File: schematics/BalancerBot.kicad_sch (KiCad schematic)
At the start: 12 parts, among them M3 Motor_Servo, M4 Motor_Servo, SW1 SW_SPDT, SW2 SW_Push, U1 ICM-20948

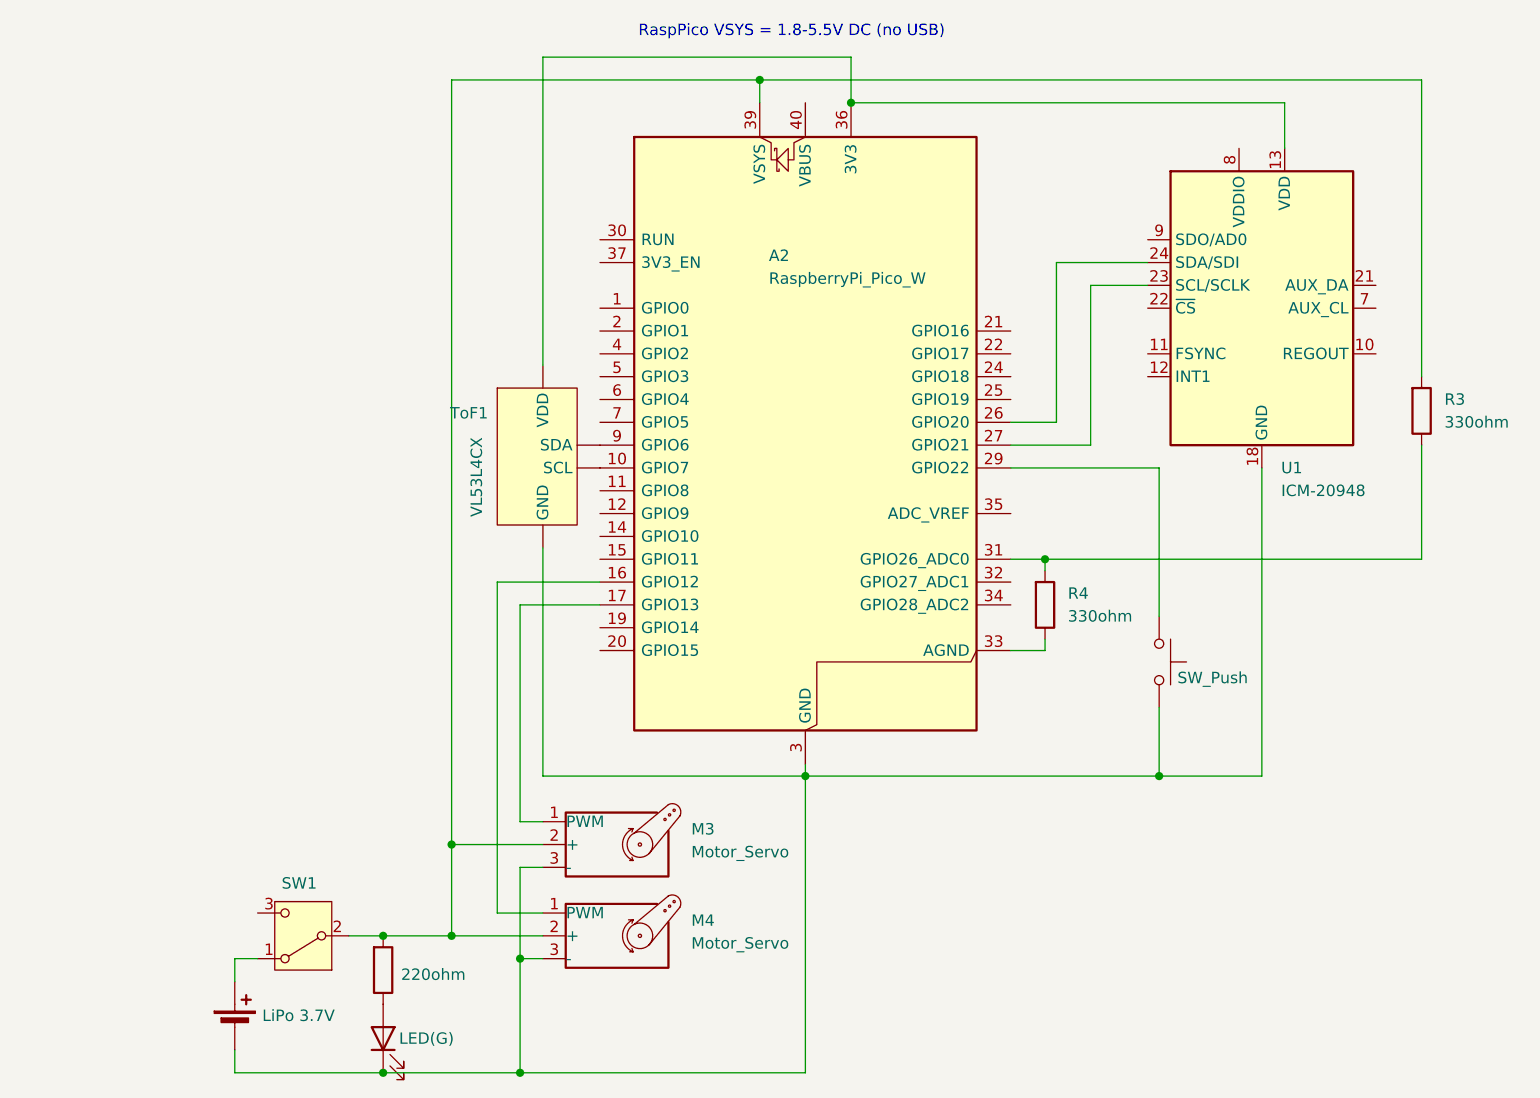
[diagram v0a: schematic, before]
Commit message: Speaker integration
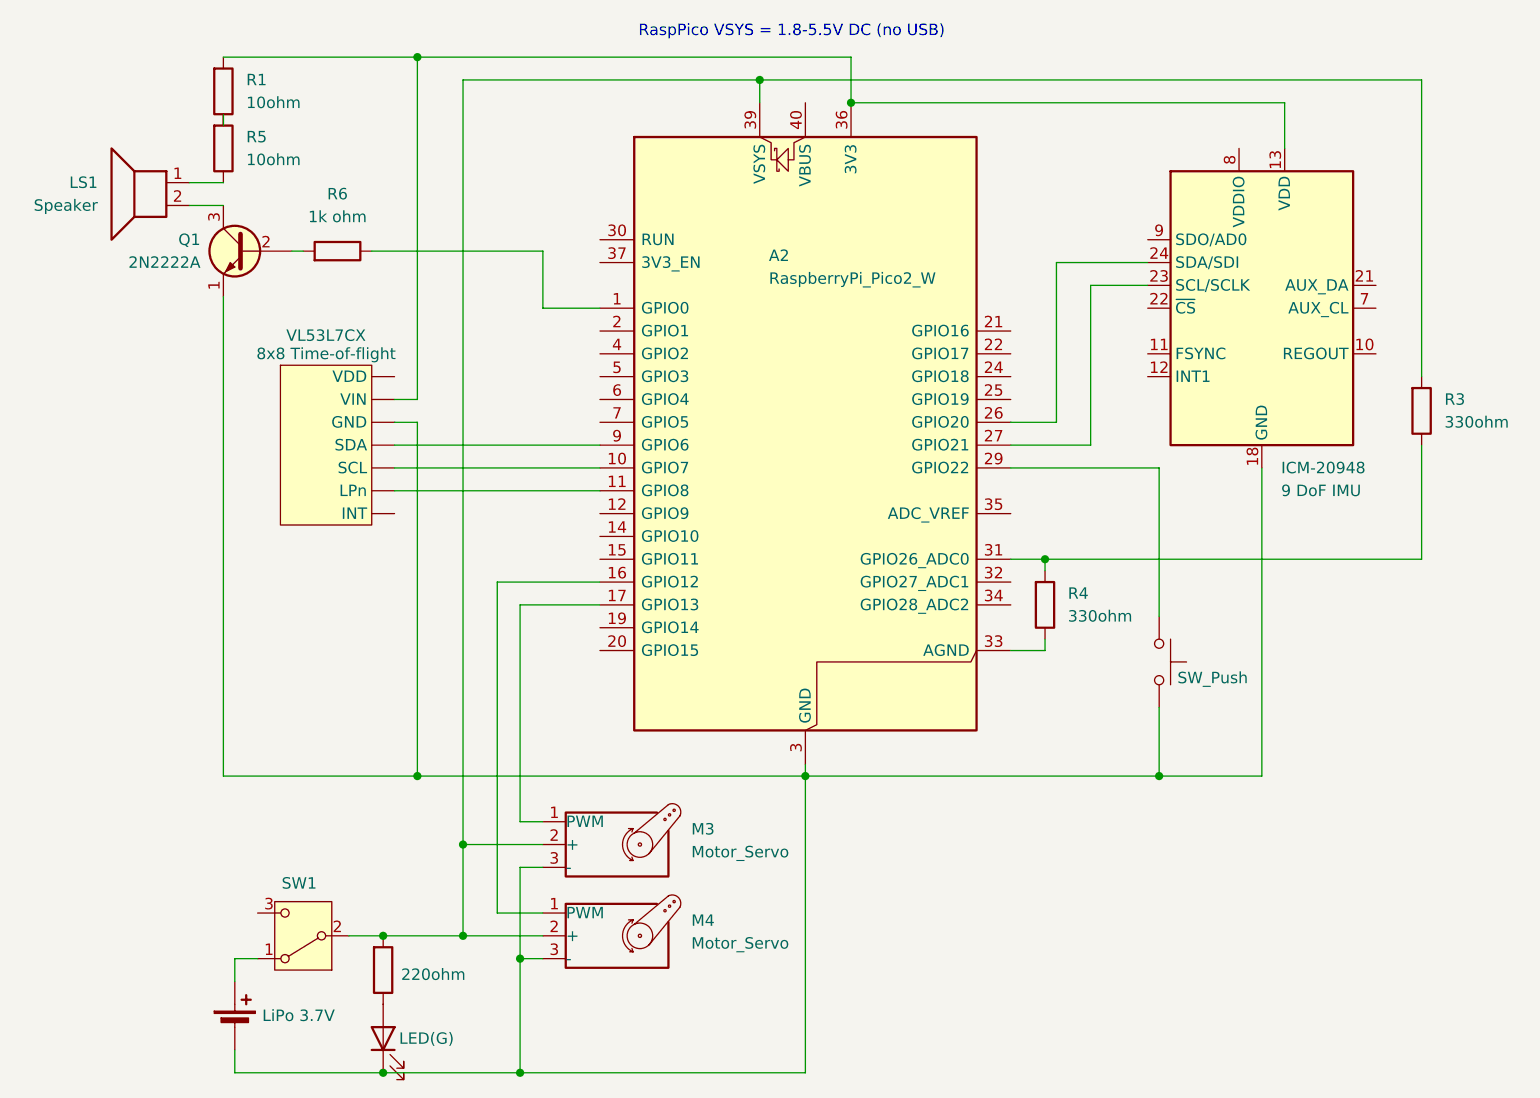
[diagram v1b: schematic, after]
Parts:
- removed ToF1: VL53L4CX, symbol 1MyLibrary:VL53L4CX
- added LS1: Speaker, symbol Device:Speaker
- added Q1: 2N2222A, PCM_Package_TO_SOT_THT_AKL:TO-18-3_EBC, symbol PCM_Transistor_BJT_AKL:2N2222A
- added R1, R5: 10ohm, symbol PCM_Resistor_AKL:R_Generic
- added R6: 1k ohm, symbol PCM_Resistor_AKL:R_Generic
- added VL53L7CX: 8x8 Time-of-flight, symbol 1MyLibrary:VL53L7CX-ToF
- A2: value RaspberryPi_Pico_W -> RaspberryPi_Pico2_W
- ICM-20948: renamed from U1; value ICM-20948 -> 9 DoF IMU
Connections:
- net at A2.36 (3V3), ICM-20948.13 (VDD): now also R1.1, VL53L7CX. (INT)
- net at A2.13 (GND), A2.18 (GND), A2.23 (GND)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: now also Q1.1 (E), VL53L7CX. (INT)
- net at A2.10 (GPIO7): now also VL53L7CX. (INT)
- net at A2.9 (GPIO6): now also VL53L7CX. (INT)
- net at A2.1 (GPIO0): now also R6.2
- net at A2.11 (GPIO8): now also VL53L7CX. (INT)
- new net: Q1.2 (B), R6.1
- new net: LS1.2, Q1.3 (C)
- new net: R1.2, R5.1
- new net: LS1.1, R5.2
